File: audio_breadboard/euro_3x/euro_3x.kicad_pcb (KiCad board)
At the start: 2 copper layers, 182.9 x 121.9 mm, 39 parts, among them J1 EURO POWER, J10 IN, J11 IN, J12 OUT, J13 OUT, J14 AUX1, J15 AUX2, J16 IN, J17 OUT, J18 GND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

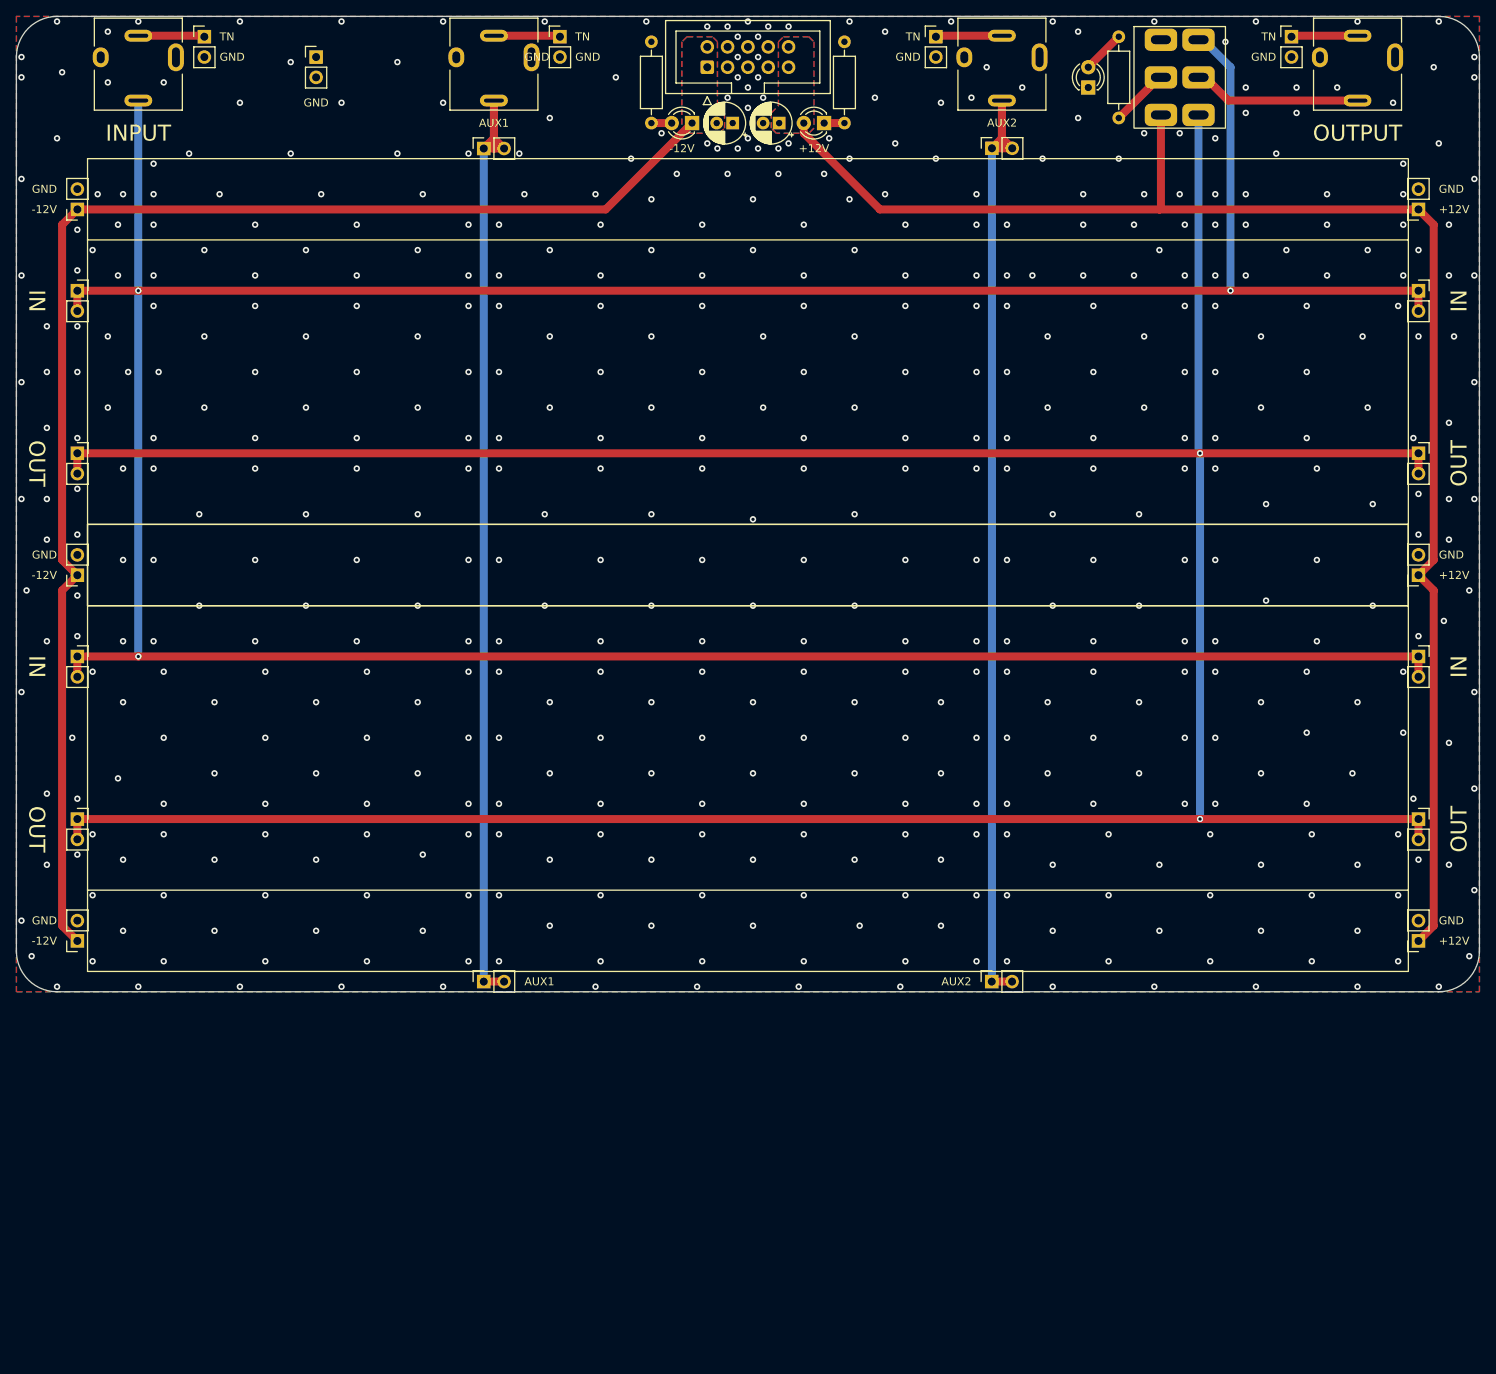
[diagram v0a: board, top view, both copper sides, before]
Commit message: start euro 3x layout
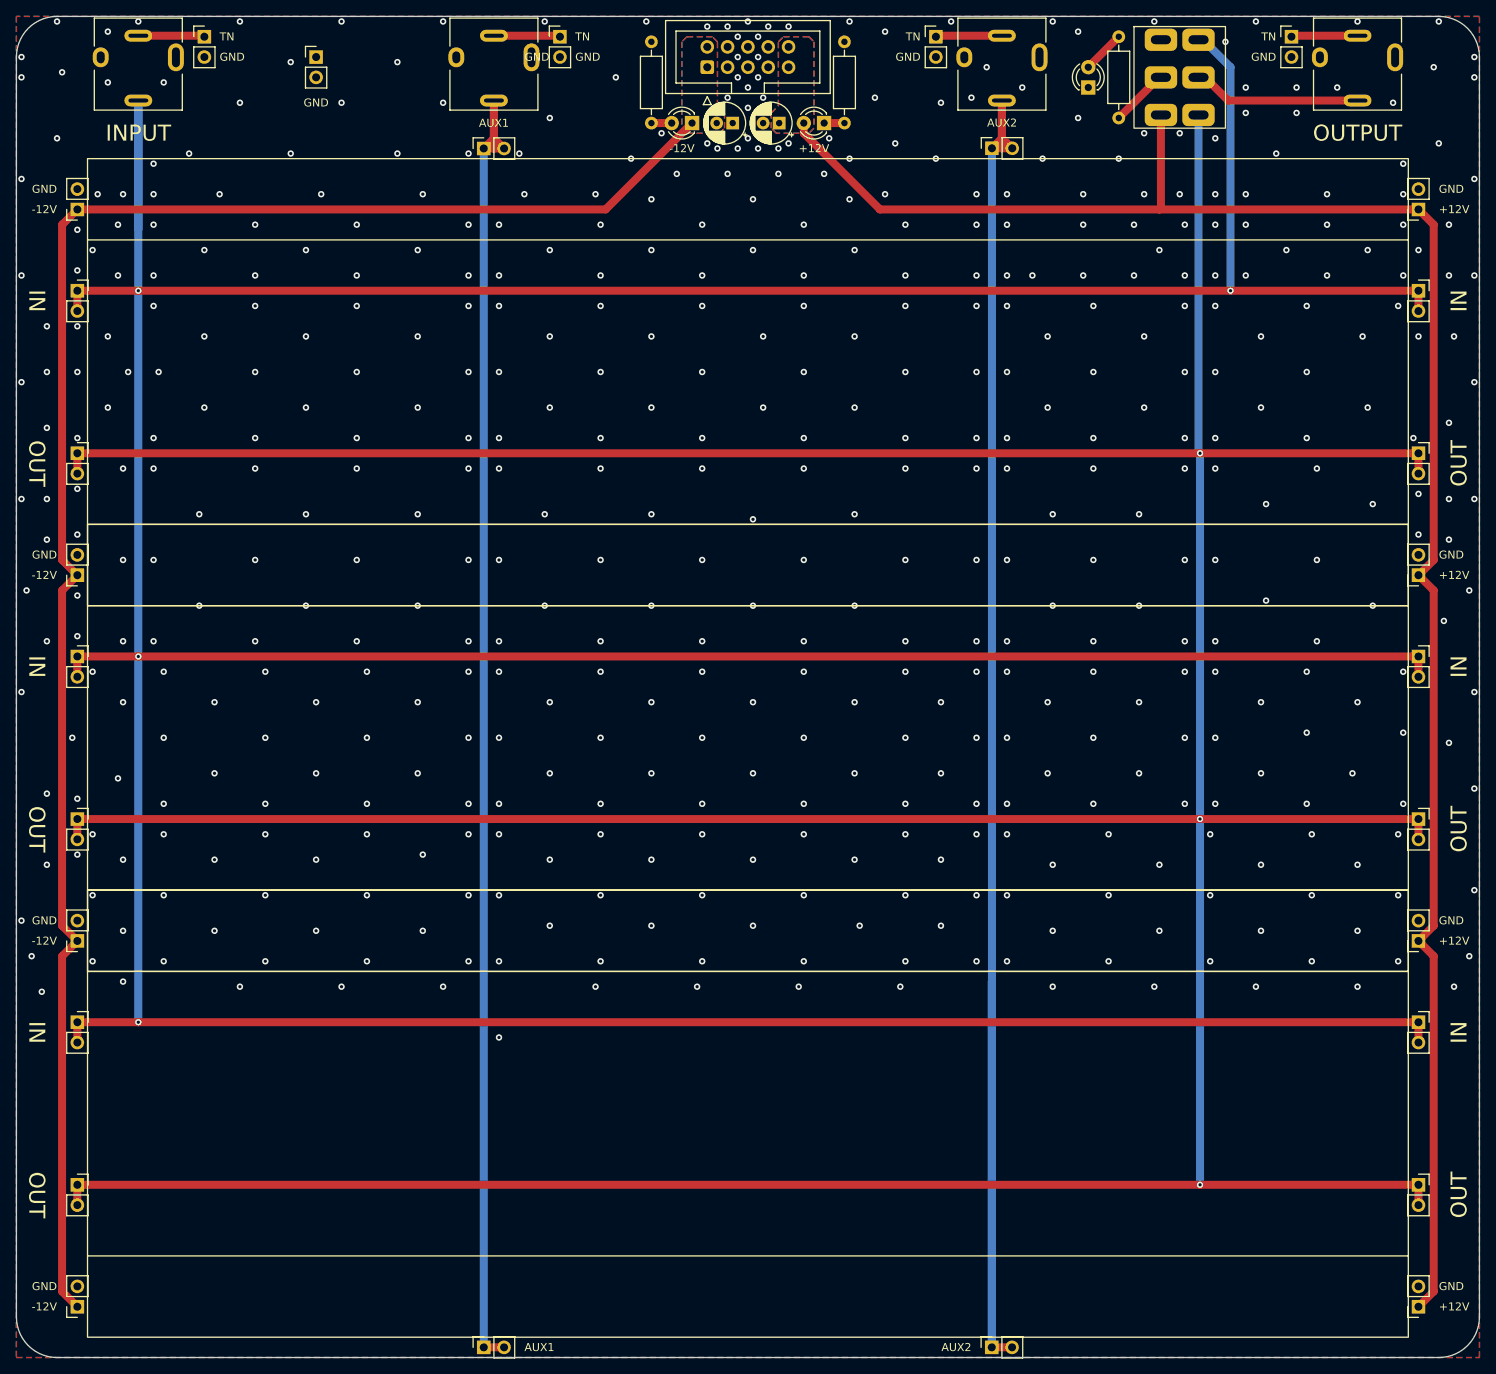
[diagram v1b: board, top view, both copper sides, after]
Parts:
- added B3: ~, kosmo-lib:Breadboard, F.Cu at (152.4, 167.6)
- added J27: IN, Connector_PinSocket_2.54mm:PinSocket_1x02_P2.54mm_Vertical, F.Cu at (68.6, 156.2)
- added J28: IN, Connector_PinSocket_2.54mm:PinSocket_1x02_P2.54mm_Vertical, F.Cu at (236.2, 156.2)
- added J29: OUT, Connector_PinSocket_2.54mm:PinSocket_1x02_P2.54mm_Vertical, F.Cu at (236.2, 176.5)
- added J30: OUT, Connector_PinSocket_2.54mm:PinSocket_1x02_P2.54mm_Vertical, F.Cu at (68.6, 176.5)
- added J31: +12V, Connector_PinSocket_2.54mm:PinSocket_1x02_P2.54mm_Vertical, F.Cu at (236.2, 191.8)
- added J32: -12V, Connector_PinSocket_2.54mm:PinSocket_1x02_P2.54mm_Vertical, F.Cu at (68.6, 191.8)
- moved J23 45.7 mm to (119.4, 196.8)
- moved J24 45.7 mm to (182.9, 196.8)
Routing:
- net /INPUT: track 448.3 -> 682.9 mm, vias 3 -> 4
- net /TO_OUT: track 433.5 -> 652.0 mm, vias 2 -> 3
- net /AUX2: track 123.5 -> 215.0 mm
- net +12V: track 188.5 -> 235.8 mm
- net -12V: track 175.9 -> 223.2 mm
- net /AUX1: track 123.5 -> 169.3 mm
- net GND: vias 519 -> 518
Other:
- board size 182.9 x 121.9 mm -> 182.9 x 167.6 mm

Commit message: fix breadboard footprint
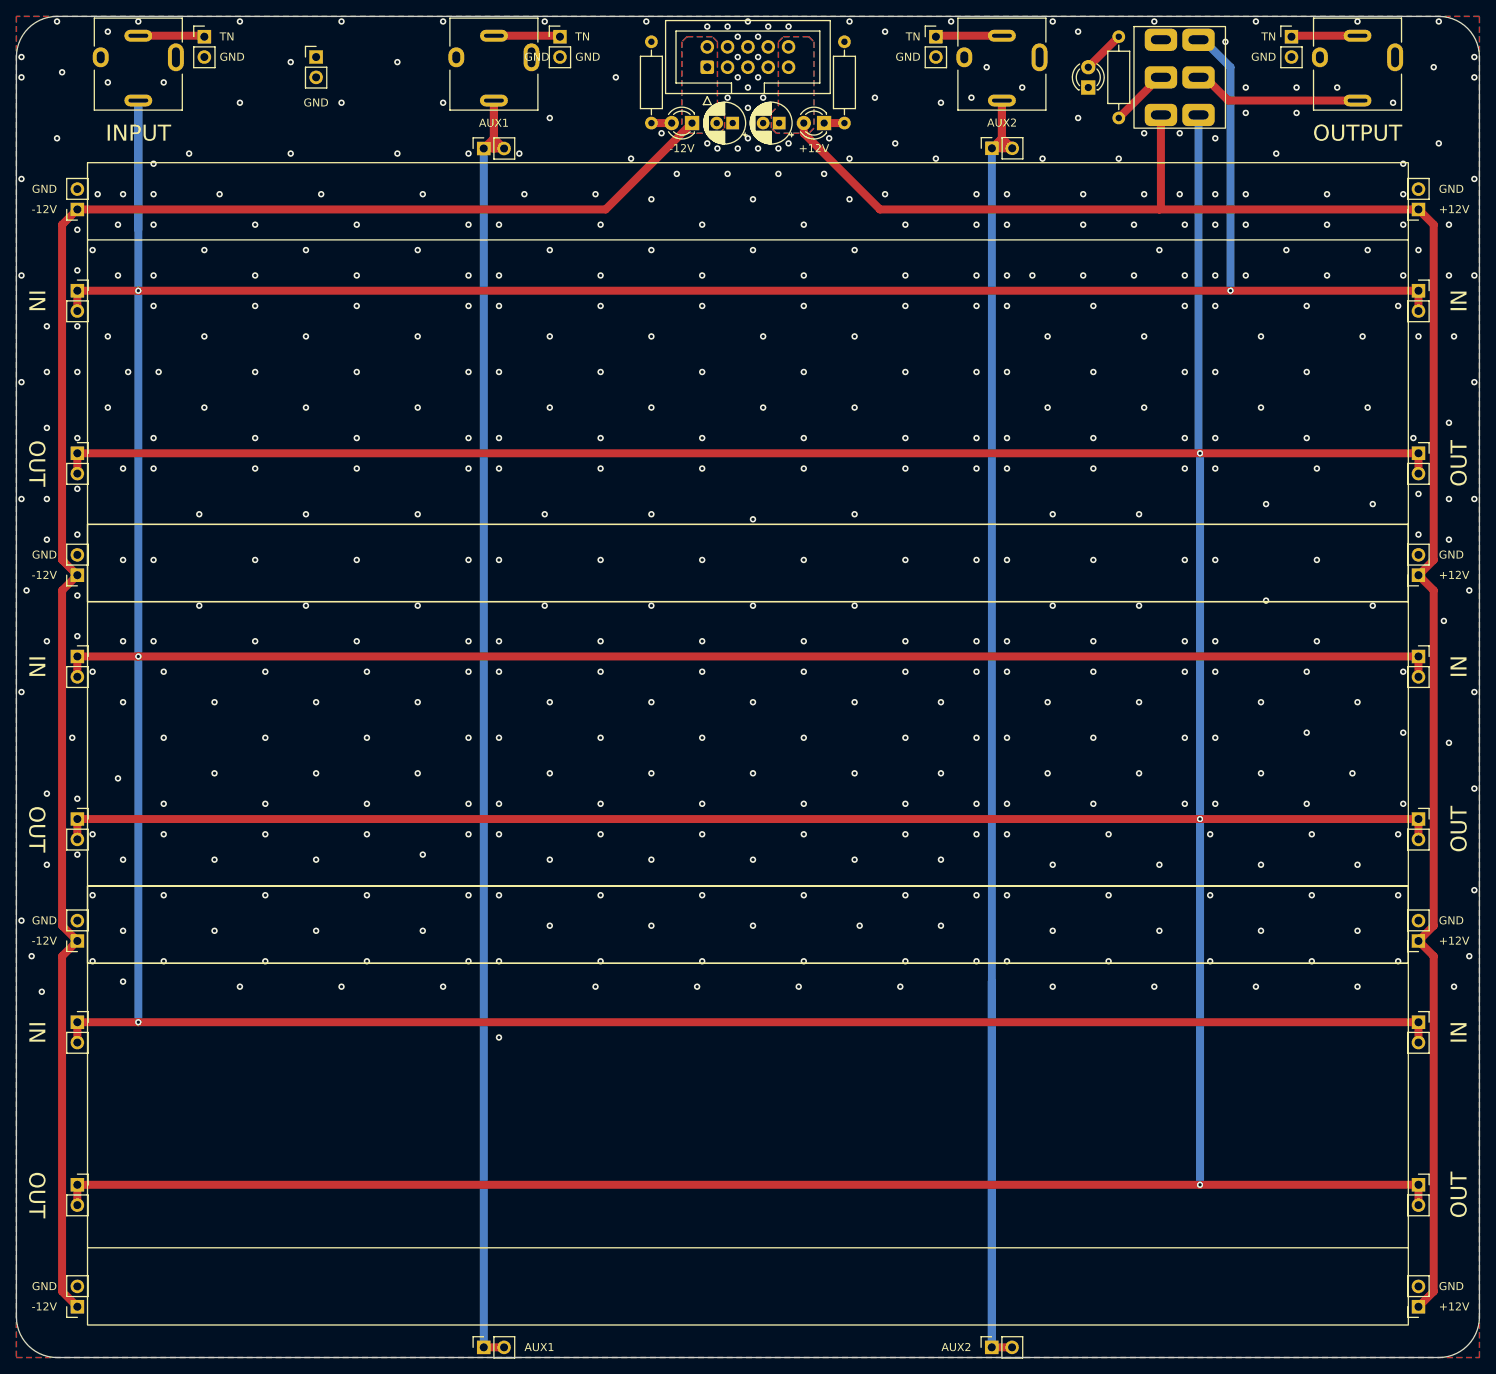
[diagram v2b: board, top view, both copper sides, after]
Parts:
- moved B3 1.02 mm to (152.4, 166.6)
- moved B2 0.51 mm to (152.4, 121.4)

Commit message: Finalize board layouts
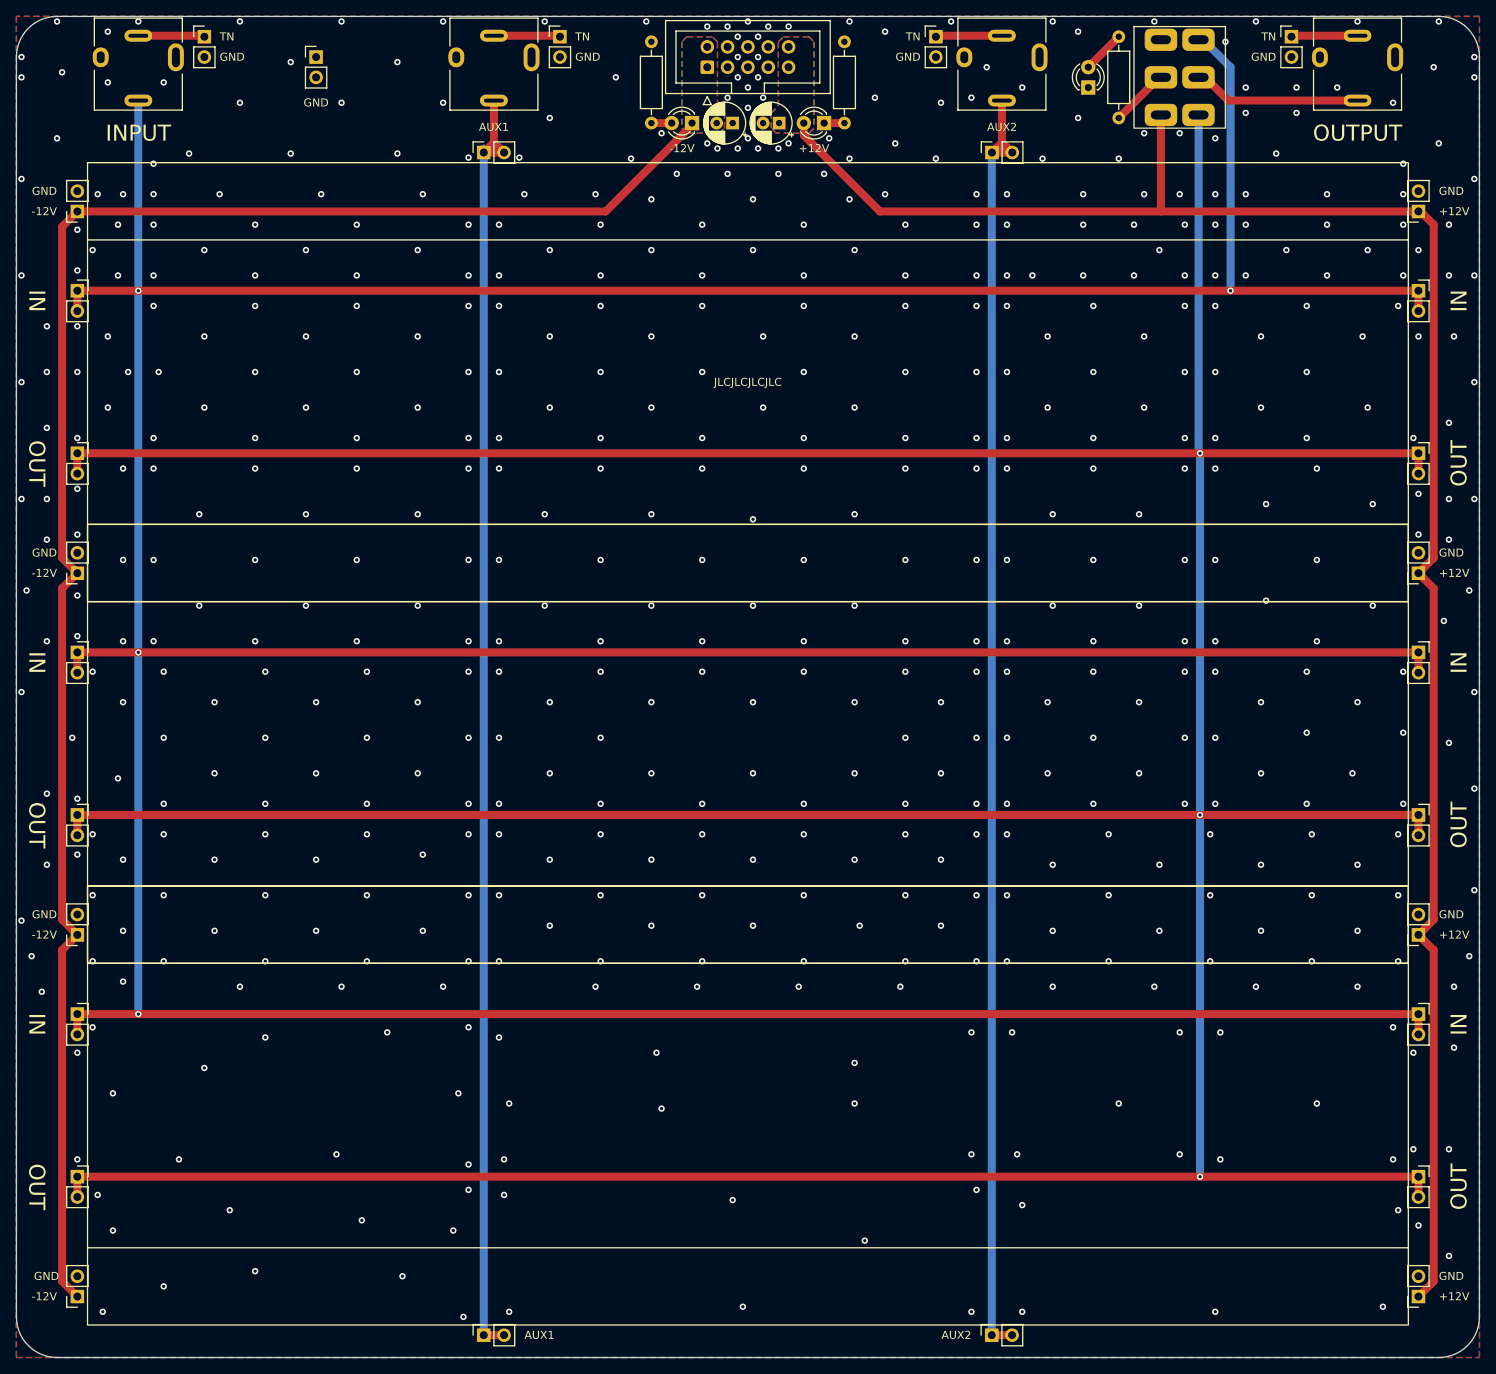
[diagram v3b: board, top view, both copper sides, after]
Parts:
- moved J23 1.52 mm to (119.4, 195.3)
- moved J24 1.52 mm to (182.9, 195.3)
- moved J31 1.27 mm to (236.2, 190.5)
- moved J32 1.27 mm to (68.6, 190.5)
- moved J27 1.02 mm to (68.6, 155.2)
- moved J28 1.02 mm to (236.2, 155.2)
- moved J29 1.02 mm to (236.2, 175.5)
- moved J30 1.02 mm to (68.6, 175.5)
- moved J19 0.76 mm to (236.2, 145.3)
- moved J20 0.76 mm to (68.6, 145.3)
- moved J15 0.53 mm to (182.9, 47.5)
- moved J17 0.51 mm to (236.2, 130.3)
- moved J22 0.51 mm to (68.6, 130.3)
- moved J14 0.51 mm to (119.4, 47.5)
- moved J16 0.51 mm to (236.2, 110.0)
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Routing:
- net /AUX2: track 215.0 -> 162.5 mm
- net /INPUT: track 682.9 -> 665.7 mm
- net /AUX1: track 169.3 -> 163.5 mm
- net -12V: track 223.2 -> 221.9 mm
- net +12V: track 235.8 -> 234.6 mm
- net /TO_OUT: track 652.0 -> 651.0 mm
- net GND: vias 518 -> 575
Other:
- board text added: "Audio Breadboard 3x Max Proskauer Jan 2024 v0.1 github.com/mprosk/audio_breadboard"
- board text added: "JLCJLCJLCJLC"
